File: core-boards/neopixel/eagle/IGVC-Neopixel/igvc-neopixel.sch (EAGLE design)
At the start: 36 parts, among them IC1 RT8289, IC2 ATMEGA8, J4 4-PIN_2MM-H, SW1 SPST_TACT-EVQQ2, U3 MCP2551T-I/SN, X1 MSTBA2, X2 16MHz

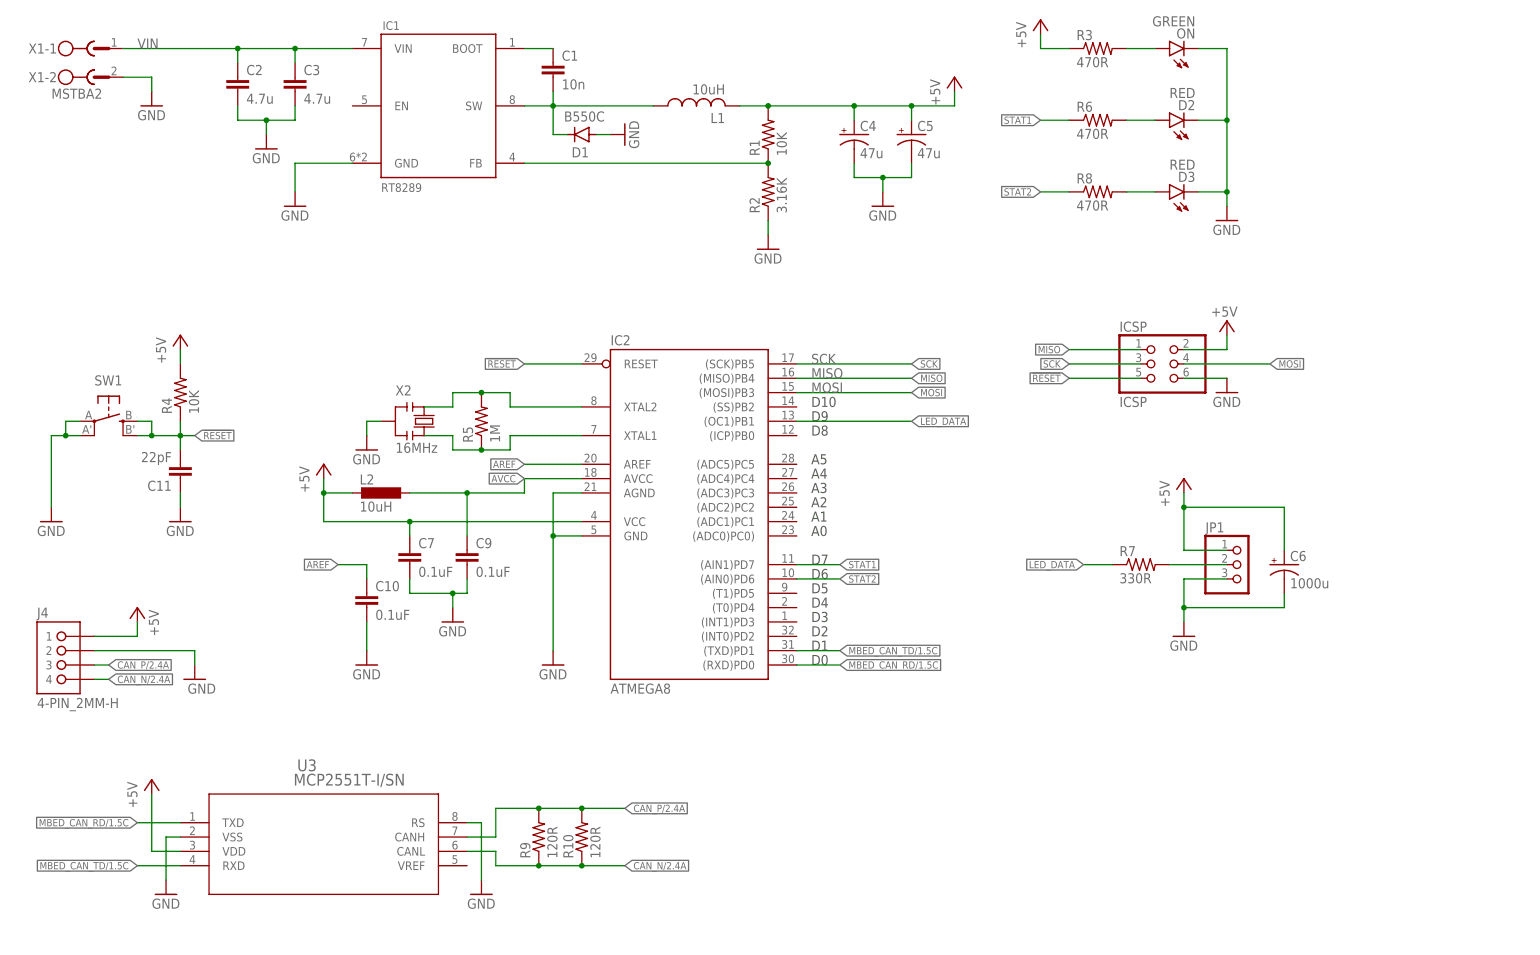
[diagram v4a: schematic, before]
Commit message: Routing neopixel
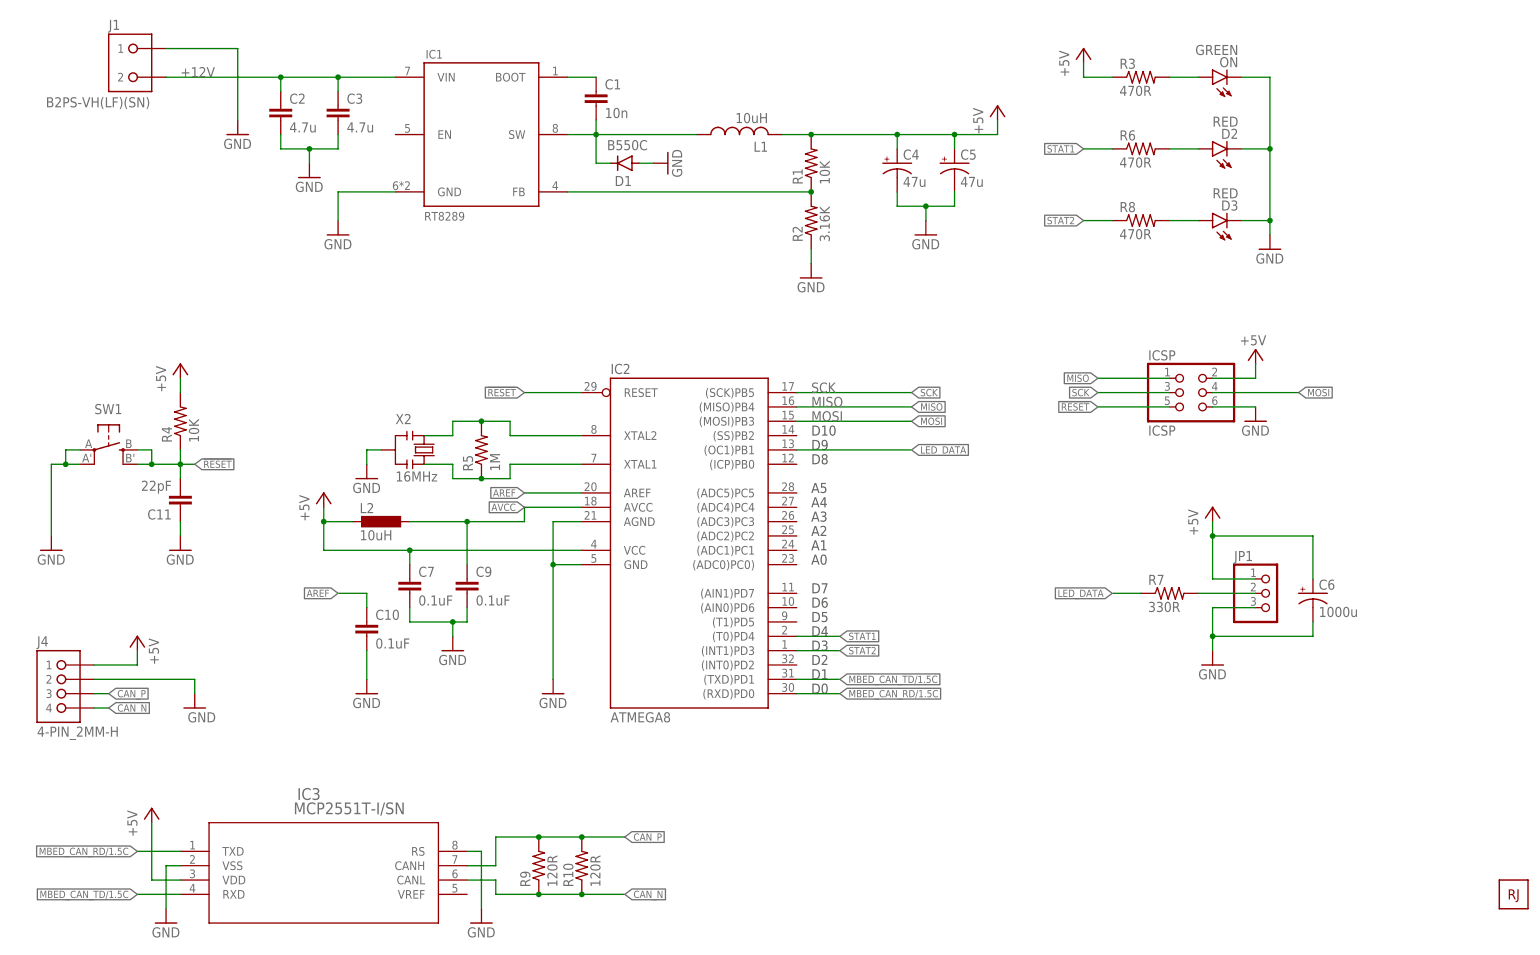
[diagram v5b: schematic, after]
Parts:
- removed U3: MCP2551T-I/SN, MCP2551T:MCP2551T-I/SN
- removed X1: MSTBA2, con-phoenix-508:MSTBA2
- added IC3: MCP2551T-I/SN, MCP2551T:MCP2551T-I/SN
- added J1: B2PS-VH(LF)(SN), RoboJackets-Connectors:B2PS-VH(LF)(SN)
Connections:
- removed net CAN_N/2.4A: J4.4, R10.1, R9.1, U3.CANL
- removed net CAN_P/2.4A: J4.3, R10.2, R9.2, U3.CANH
- removed net VIN: C2.1, C3.1, IC1.VIN, X1-1.1
- new net +12V: C2.1, C3.1, IC1.VIN, J1.2
- new net CAN_N: IC3.CANL, J4.4, R10.1, R9.1
- new net CAN_P: IC3.CANH, J4.3, R10.2, R9.2
- net +5V: now also IC3.VDD; no longer U3.VDD
- net GND: now also IC3.RS, IC3.VSS, J1.1; no longer U3.RS, U3.VSS, X1-2.1
- net MBED_CAN_RD/1.5C: now also IC3.TXD; no longer U3.TXD
- net MBED_CAN_TD/1.5C: now also IC3.RXD; no longer U3.RXD
- net STAT1: now also IC2.(T0)PD4; no longer IC2.(AIN1)PD7
- net STAT2: now also IC2.(INT1)PD3; no longer IC2.(AIN0)PD6
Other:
- moved on the sheet: C1, C10, C11, C2, C3, C4, C5, C6, C7, C9, D1, D2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

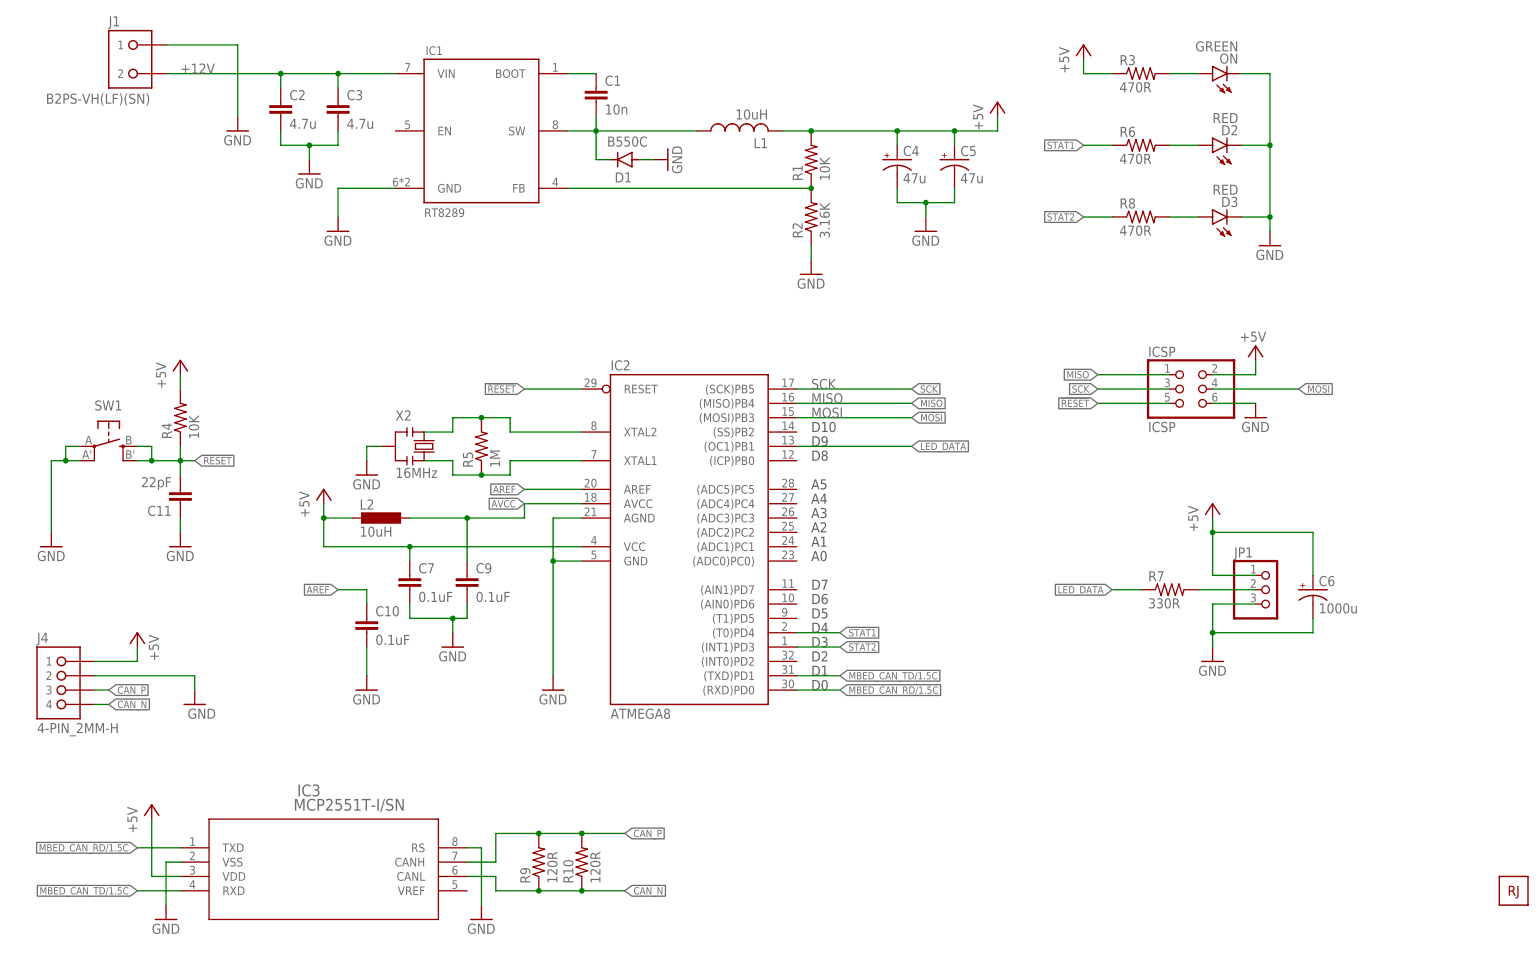
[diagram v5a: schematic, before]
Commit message: Routed neopixel
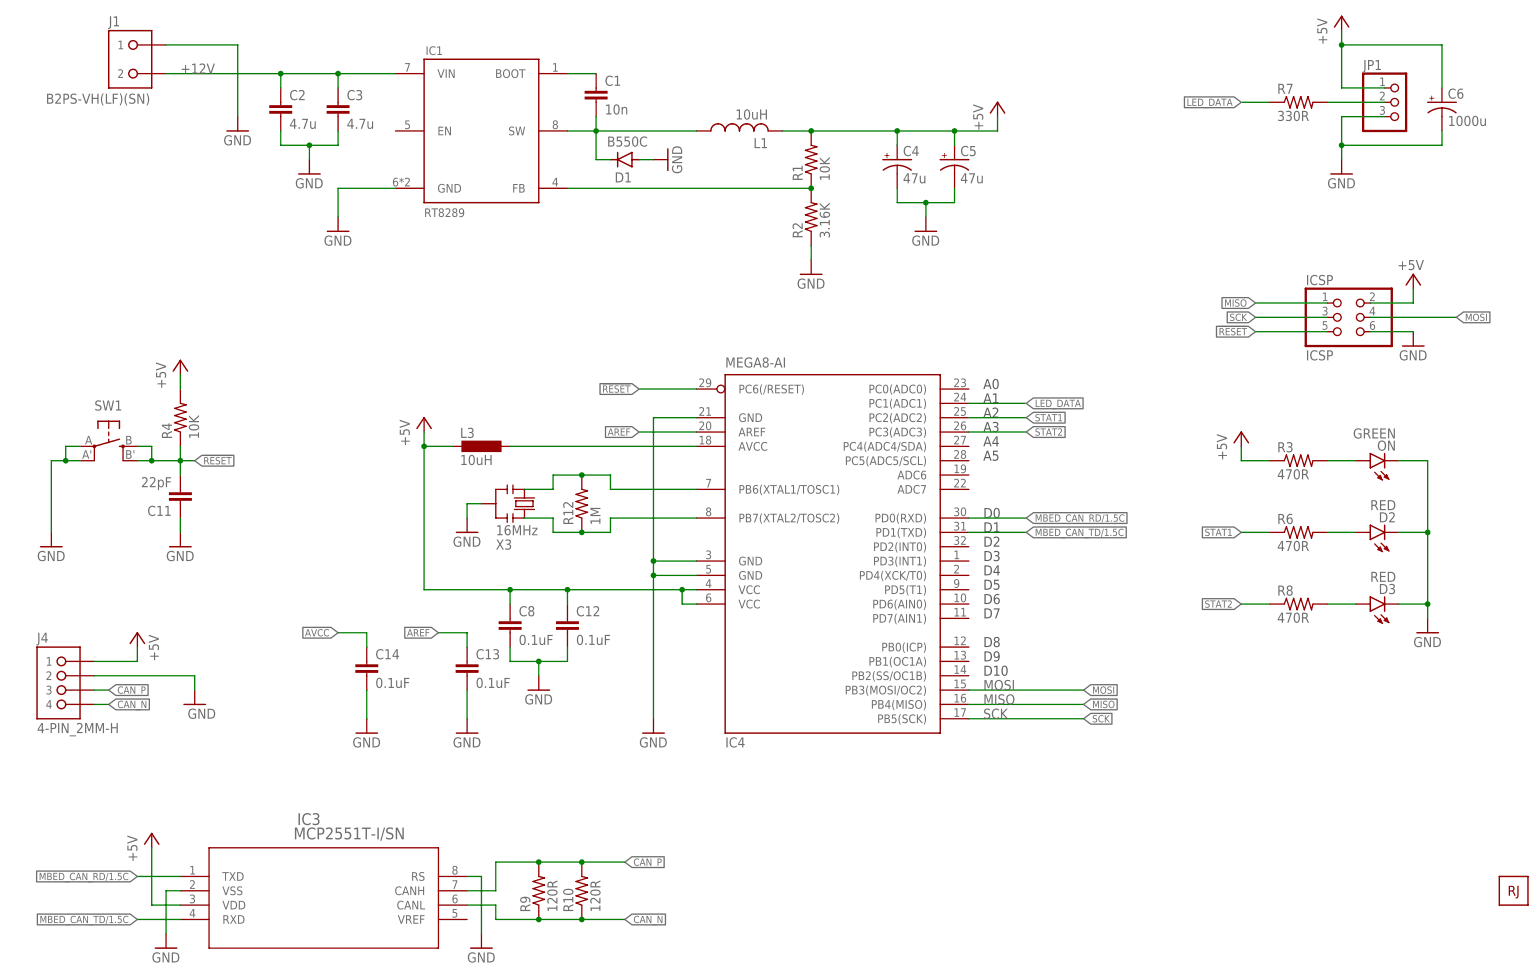
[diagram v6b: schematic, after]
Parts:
- removed C10, C7, C9: 0.1uF, resistor:C-EUC0603
- removed IC2: ATMEGA8, atmel:AT90S4433A
- removed L2: 10uH, IGVC-Remote:L-0805
- removed R5: 1M, resistor:R-US_R0603
- removed X2: 16MHz, IGVC-Remote:OSC_CSTCE16M0V53-R0
- added C12, C13, C14, C8: 0.1uF, resistor:C-EUC0603
- added IC4: MEGA8-AI, atmel:MEGA8-AI
- added L3: 10uH, IGVC-Remote:L-0805
- added R12: 1M, resistor:R-US_R0603
- added X3: 16MHz, IGVC-Remote:OSC_CSTCE16M0V53-R0
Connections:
- removed net XTAL1: IC2.XTAL1, R5.1, X2.3
- removed net XTAL2: IC2.XTAL2, R5.2, X2.1
- new net XTAL5: IC4.PB6(XTAL1/TOSC1), R12.2, X3.1
- new net XTAL6: IC4.PB7(XTAL2/TOSC2), R12.1, X3.3
- net !RESET: now also IC4.PC6(/RESET); no longer IC2.RESET
- net +5V: now also C12.1, C8.1, IC4.VCC@1, IC4.VCC@2, L3.2; no longer C7.1, IC2.VCC, L2.2
- net AREF: now also C13.1, IC4.AREF; no longer C10.1, IC2.AREF
- net AVCC: now also C14.1, IC4.AVCC, L3.1; no longer C9.1, IC2.AVCC, L2.1
- net GND: now also C12.2, C13.2, C14.2, C8.2, IC4.GND, IC4.GND@1, IC4.GND@2, X3.2; no longer C10.2, C7.2, C9.2, IC2.AGND, IC2.GND, X2.2
- net LED_DATA: now also IC4.PC1(ADC1); no longer IC2.(OC1)PB1
- net MBED_CAN_RD/1.5C: now also IC4.PD0(RXD); no longer IC2.(RXD)PD0
- net MBED_CAN_TD/1.5C: now also IC4.PD1(TXD); no longer IC2.(TXD)PD1
- net MISO: now also IC4.PB4(MISO); no longer IC2.(MISO)PB4
- net MOSI: now also IC4.PB3(MOSI/OC2); no longer IC2.(MOSI)PB3
- net SCK: now also IC4.PB5(SCK); no longer IC2.(SCK)PB5
- net STAT1: now also IC4.PC2(ADC2); no longer IC2.(T0)PD4
- net STAT2: now also IC4.PC3(ADC3); no longer IC2.(INT1)PD3
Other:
- moved on the sheet: C6, D2, D3, IC3, ICSP, JP1, ON, R10, R3, R6, R7, R8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
